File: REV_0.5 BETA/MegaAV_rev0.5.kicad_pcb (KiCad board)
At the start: 4 copper layers, 50 x 50 mm, 170 parts, among them CN1 MD-90SM_MD2, P1 SMD_Conn_01x01, U1 4070, U2 74HCT123, U3 TS924, U4 THS7374, U5 ICS501, U6 TS922, U7 TS924, U8 AD725

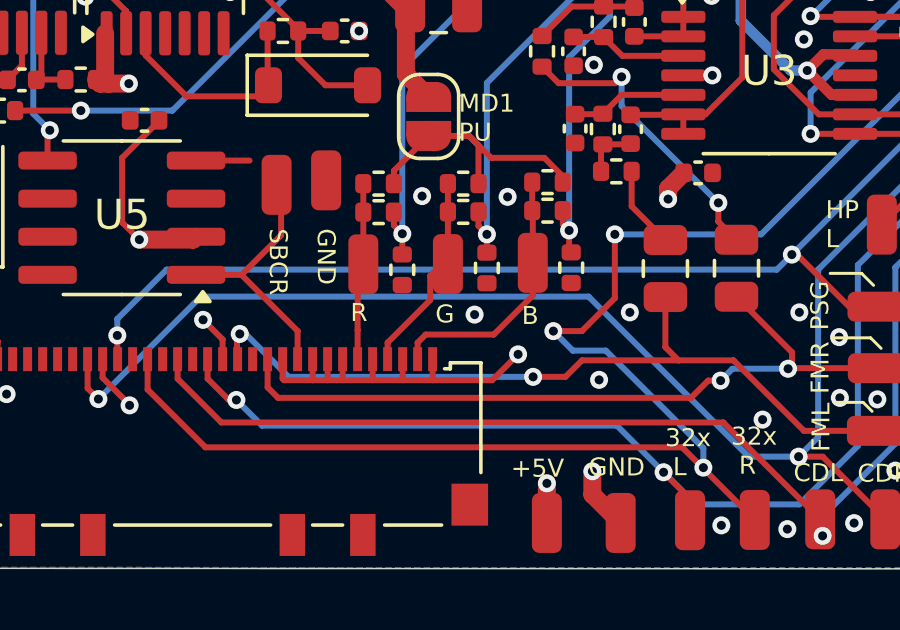
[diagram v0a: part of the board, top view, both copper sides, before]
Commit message: optimized luma trap values & PSG fix. Some silscreening to.
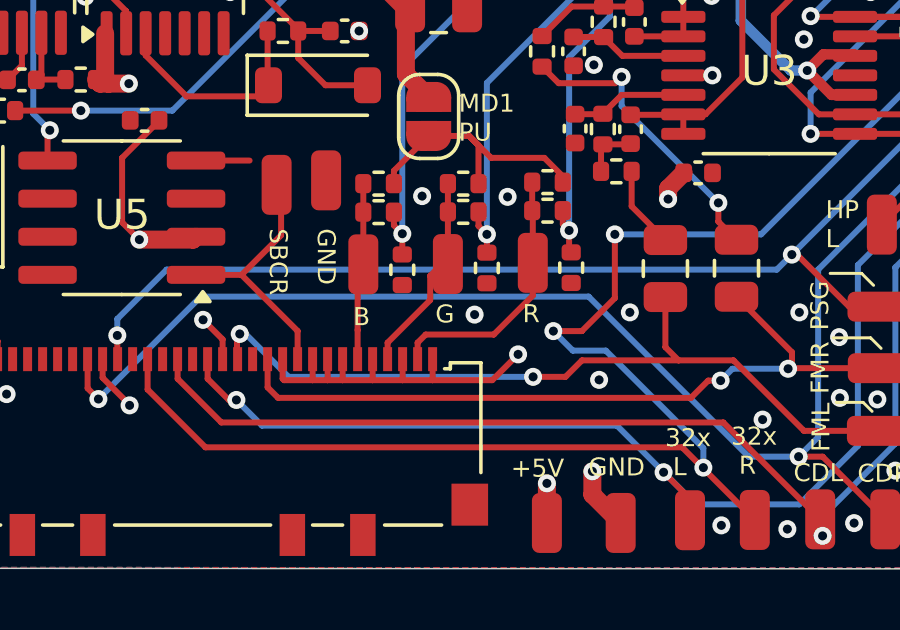
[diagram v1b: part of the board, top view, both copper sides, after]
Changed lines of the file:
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@@
 	)
 	(gr_text "B"
-		(at 190.67 136.26 0)
+		(at 185.05 136.3 0)
 		(layer "F.SilkS")
 		(effects
@@
 	)
 	(gr_text "R"
-		(at 184.96 136.16 0)
+		(at 190.7 136.2 0)
 		(layer "F.SilkS")
 		(effects

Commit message: Fixed jumper silkscreening
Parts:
- moved G*** 3.10 mm to (179.3, 122.7)
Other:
- board text added: "JUMPER SETTINGS: MD1 VA0-6.8: 1 C MD1 VA7, MD2 VA3: 2 C MD2 VA0-1.8: 2 C D MD2 VA2-2.3: 1 B MD2 VA4: 2 A MD3: 2 A D REGION SELECT: Bridge PAL Or NTSC Jumper If you LIFTED RGB Legs: MD1PU HEADPHONE OUT: MD1 VA0-VA6.8: Y MD1 VA7, CDX, NOMAD, MEGA JET: Z NO HEADPHONE OUT: Y & SHORT HP P1 AND HP P2"
- board text removed: "JUMPER SETTINGS: MD1 VA0-VA6.8: c, 1 MD1 VA7, MD2 VA3-VA4: a, 2 MD2 VA0-VA1.8/MD3: a, d, 2 MD2 VA2-VA2.3 b, 1 REGION SELECT: Bridge PAL Or NTSC Jumper If you LIFTED RGB Legs: MD1PU HEADPHONE OUT: MD1 VA0-VA6.8: Y MD1 VA7, CDX, NOMAD, MEGA JET: Z NO HEADPHONE OUT: MD1 VA7: SHORT HP P1 AND HP P2"
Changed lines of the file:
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@@
 	(footprint "LOGO_Library:MegaAV Logo 2"
 		(layer "B.Cu")
-		(at 182.45 122.55 90)
+		(at 179.35 122.65 90)
 		(property "Reference" "G***"
 			(at 0 0 90)
@@
 	)
 	(gr_line
-		(start 199.45 121.25)
-		(end 199.55 133.8)
+		(start 196.25 121.225)
+		(end 196.35 133.775)
 		(stroke
 			(width 0.1)
@@
 	)
 	(gr_line
-		(start 191.25 106.3)
+		(start 188.05 106.3)
 		(end 198.9 106.25)
 		(stroke
@@
 	)
 	(gr_line
-		(start 193.05 133.8)
-		(end 193.05 118.4)
+		(start 189.9 133.9)
+		(end 189.9 118.5)
 		(stroke
 			(width 0.1)
@@
 	(gr_line
 		(start 218.85 134.05)
-		(end 191.2 134.2)
+		(end 188 134.2)
 		(stroke
 			(width 0.1)
@@
 	)
 	(gr_line
-		(start 207.55 133.75)
-		(end 207.55 122.2)
+		(start 204.35 133.775)
+		(end 204.35 122.225)
 		(stroke
 			(width 0.1)
@@
 	)
 	(gr_line
-		(start 191.2 134.2)
-		(end 191.25 106.3)
+		(start 188 134.2)
+		(end 188.05 106.3)
 		(stroke
 			(width 0.1)
@@
 	)
 	(gr_line
-		(start 217.1 120.2)
-		(end 217.25 133.95)
+		(start 217.1 119.5)
+		(end 217.25 133.25)
 		(stroke
 			(width 0.1)
@@
 		)
 	)
-	(gr_text "JUMPER SETTINGS:\nMD1 VA0-VA6.8: c, 1\nMD1 VA7, MD2 VA3-VA4: a, 2\nMD2 VA0-VA1.8/MD3: a, d, 2 \nMD2 VA2-VA2.3 b, 1\n\nREGION SELECT:\nBridge PAL Or NTSC Jumper\n\nIf you LIFTED RGB Legs: MD1PU\n\nHEADPHONE OUT:\nMD1 VA0-VA6.8: Y\nMD1 VA7, CDX, NOMAD, MEGA JET: Z\n\nNO HEADPHONE OUT:\nMD1 VA7: SHORT HP P1 AND HP P2"
-		(at 191.6 134.05 270)
+	(gr_text " JUMPER SETTINGS:\nMD1 VA0-6.8: 1 C\nMD1 VA7, MD2 VA3: 2 C\nMD2 VA0-1.8: 2 C D\nMD2 VA2-2.3: 1 B\nMD2 VA4: 2 A\nMD3: 2 A D\n\nREGION SELECT:\nBridge PAL Or NTSC Jumper\n\nIf you LIFTED RGB Legs: MD1PU\n\nHEADPHONE OUT:\nMD1 VA0-VA6.8: Y\nMD1 VA7, CDX, NOMAD, MEGA JET: Z\n\nNO HEADPHONE OUT:\nY & SHORT HP P1 AND HP P2"
+		(at 188.4 134.15 270)
 		(layer "B.SilkS")
 		(effects

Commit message: Changes to the liscense, readme, and silkscreening.
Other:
- board text added: "Dev Team: Villahed94 RGBeter"
- board text removed: "Dev Team: Villahed94 Ace9921 RGBeter"
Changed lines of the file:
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@@
 	)
 	(gr_line
-		(start 202 136)
-		(end 202 143.45)
+		(start 201.2 136.025)
+		(end 201.2 143.475)
 		(stroke
 			(width 0.1)
@@
 		)
 	)
-	(gr_text "Dev Team:\nVillahed94\nAce9921\nRGBeter\n"
+	(gr_text "Dev Team:\nVillahed94\nRGBeter\n"
 		(at 200.3 143.5 270)
 		(layer "B.SilkS")
